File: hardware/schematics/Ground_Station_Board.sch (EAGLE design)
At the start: 11 parts

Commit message: Add files via upload
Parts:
- C1: value 8.2pF -> 47pF
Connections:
- net N$2 renamed LED_2
- removed net N$1: R3.2, U$2.37/A18
- removed net N$3: R1.2, U$2.39/A20
- new net LED_1: R1.2, U$2.37/A18
- new net LED_3: R3.2, U$2.39/A20
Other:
- note added: "Indicator LEDS"
- moved on the sheet: C1, C2, C3, LED1, LED2, LED3, R1, R2, R3, U$1

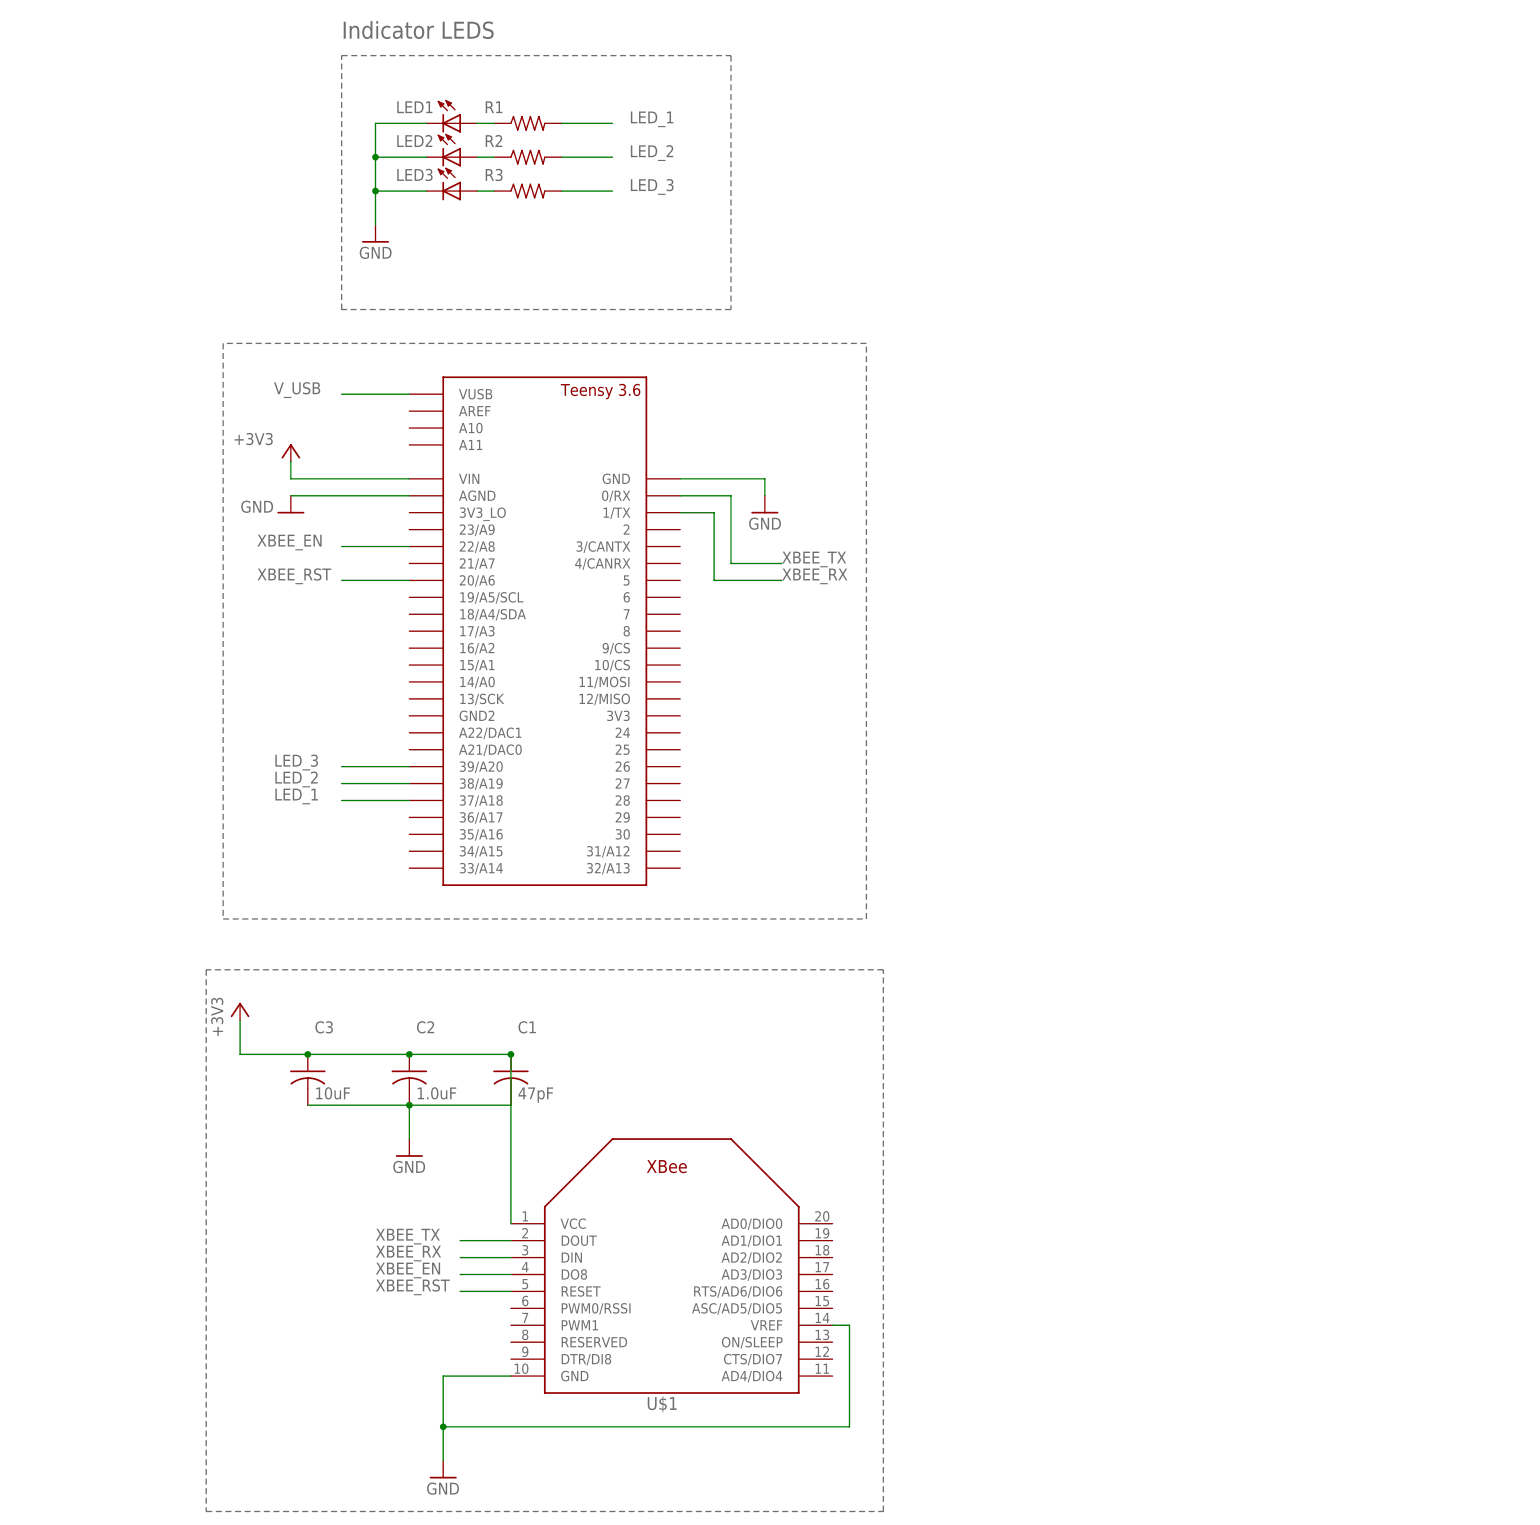
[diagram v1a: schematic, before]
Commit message: Add files via upload
Updated resistor and capacitor values
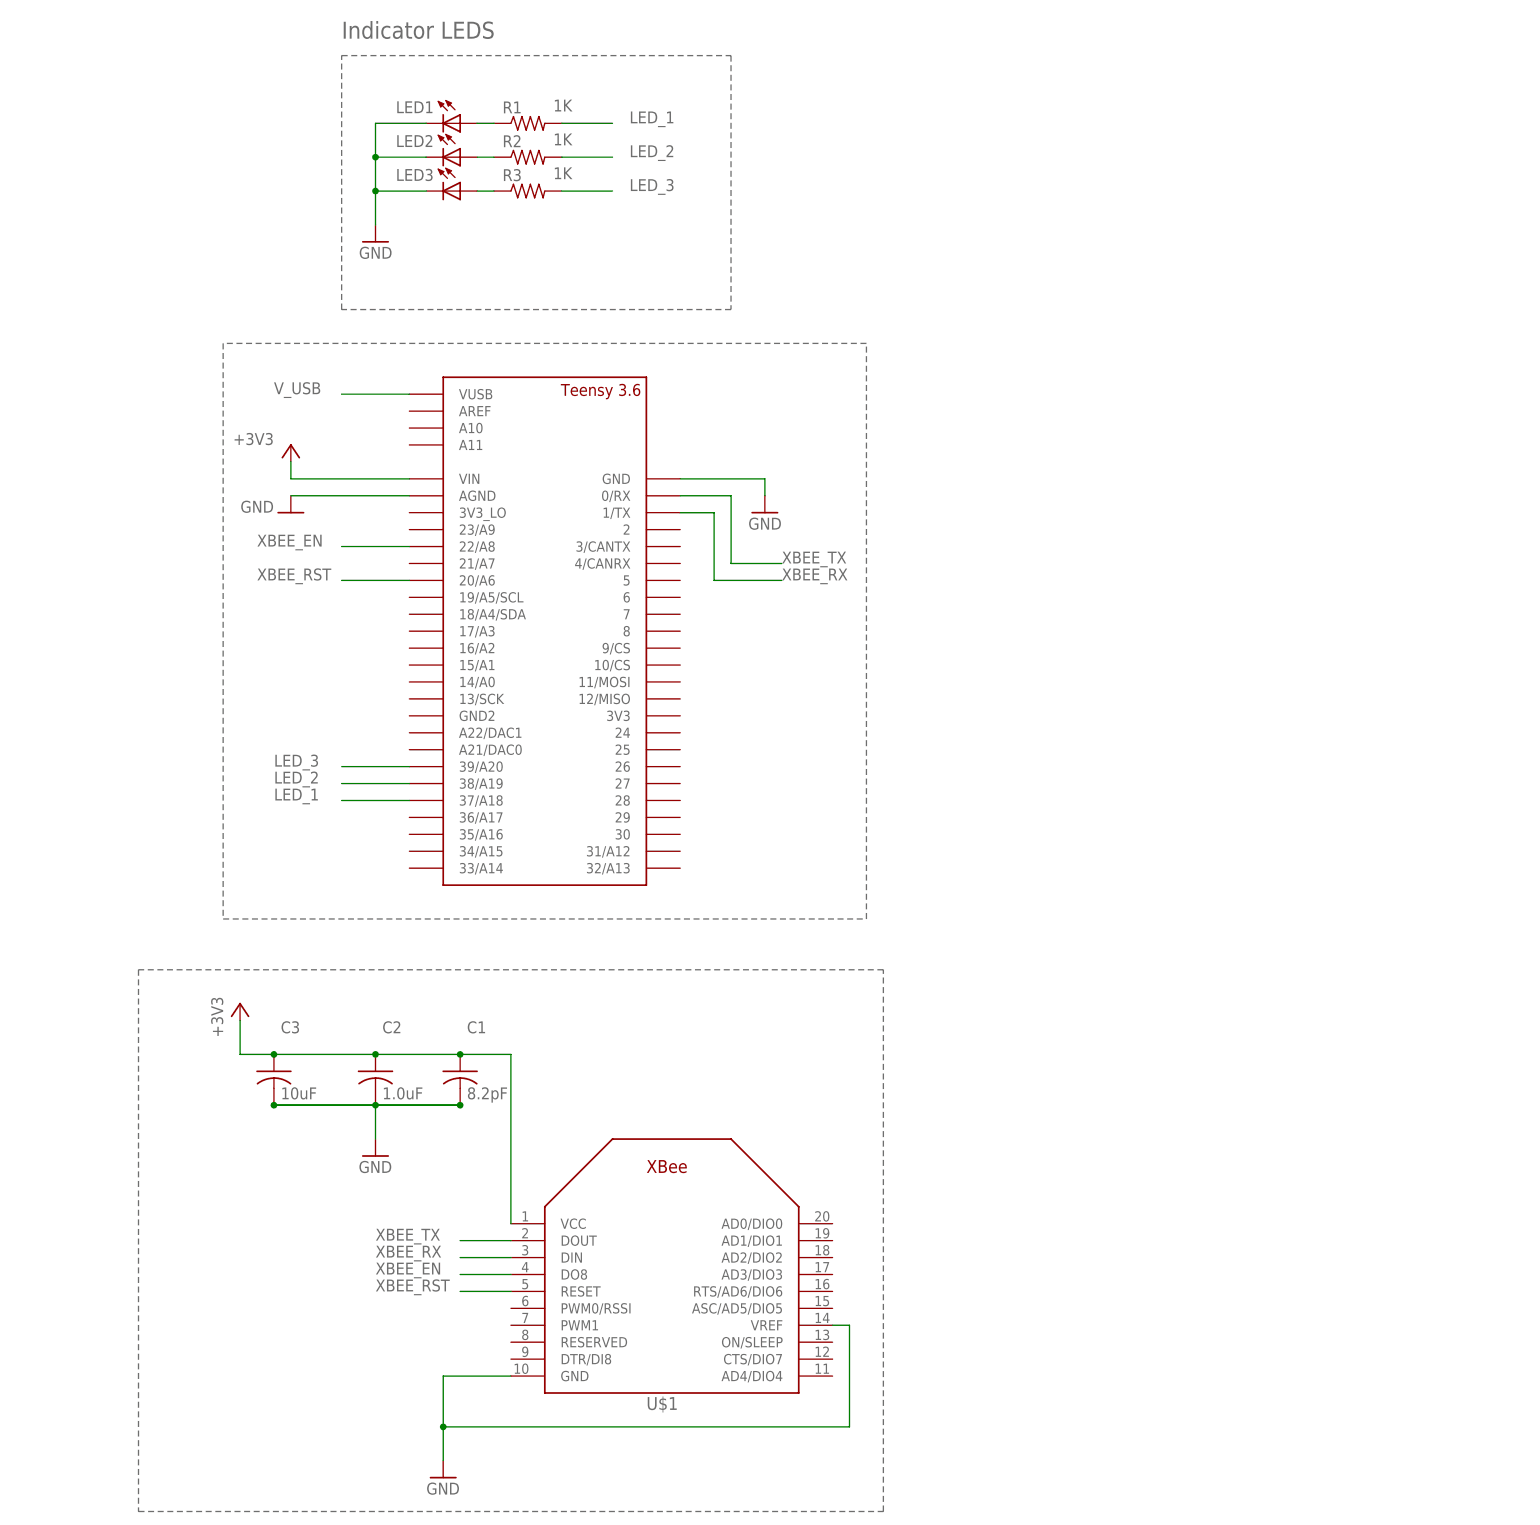
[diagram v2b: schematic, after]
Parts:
- C1: value 47pF -> 8.2pF
- R1, R2, R3: device rcl:R-US_0204/7 -> rcl:R-US_0207/7
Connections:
- removed net VCC: C1.1, C2.1, C3.1, U$1.VCC
- net +3V3: now also C1.1, C2.1, C3.1, U$1.VCC
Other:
- moved on the sheet: C1, C2, C3
